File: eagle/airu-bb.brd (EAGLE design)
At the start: 86.4 x 54.6 mm, 34 parts, among them IC1 DS1307, U1 BMP180, U2 DHT22, U3 GPS, X2 53261-08, Y1 32.768kHz

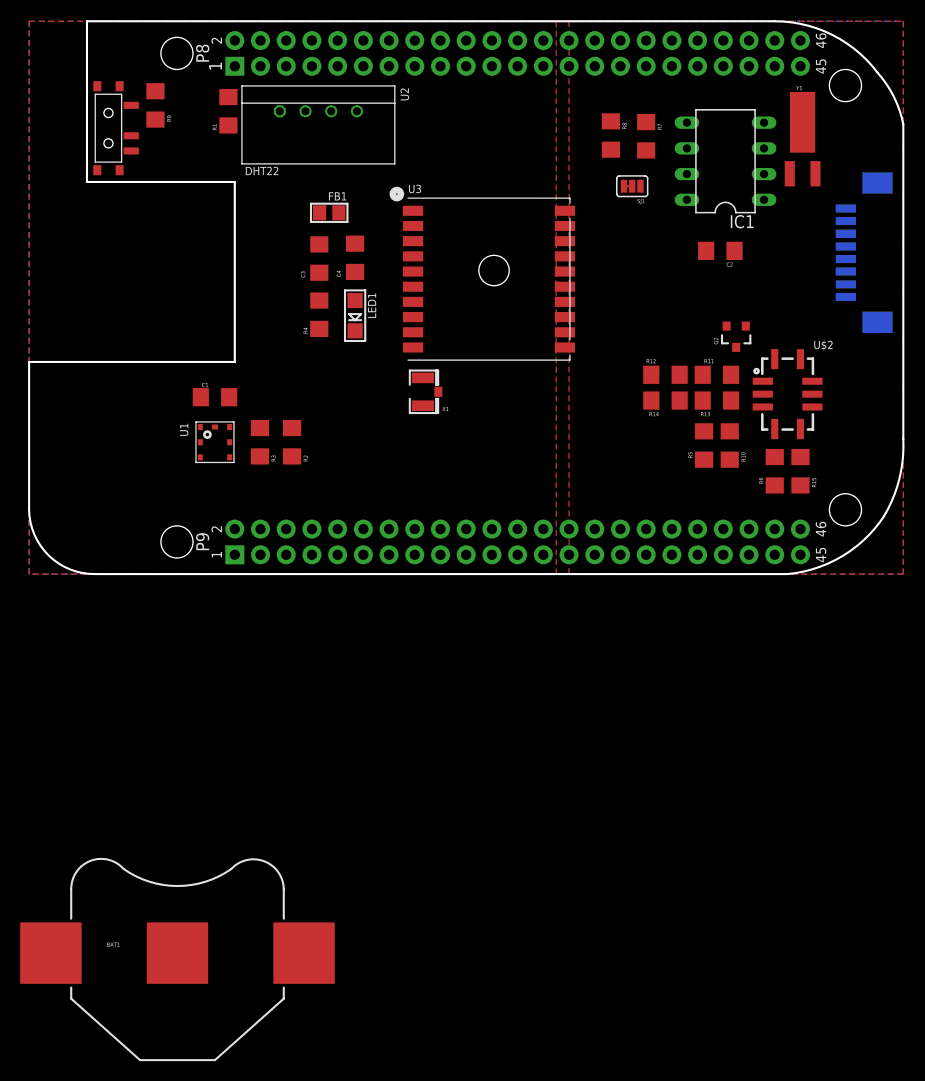
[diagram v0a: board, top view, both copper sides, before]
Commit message: Added modifications for AirU V2.0
This commit includes all modifications needed for AirU V2.0. This includes:

* Schematic additions integrating a mode button and real-time clock
* Board layout revisions to integrate the added components
* Changes to the BOM to reflect the new design

I also reorganized the repository structure.
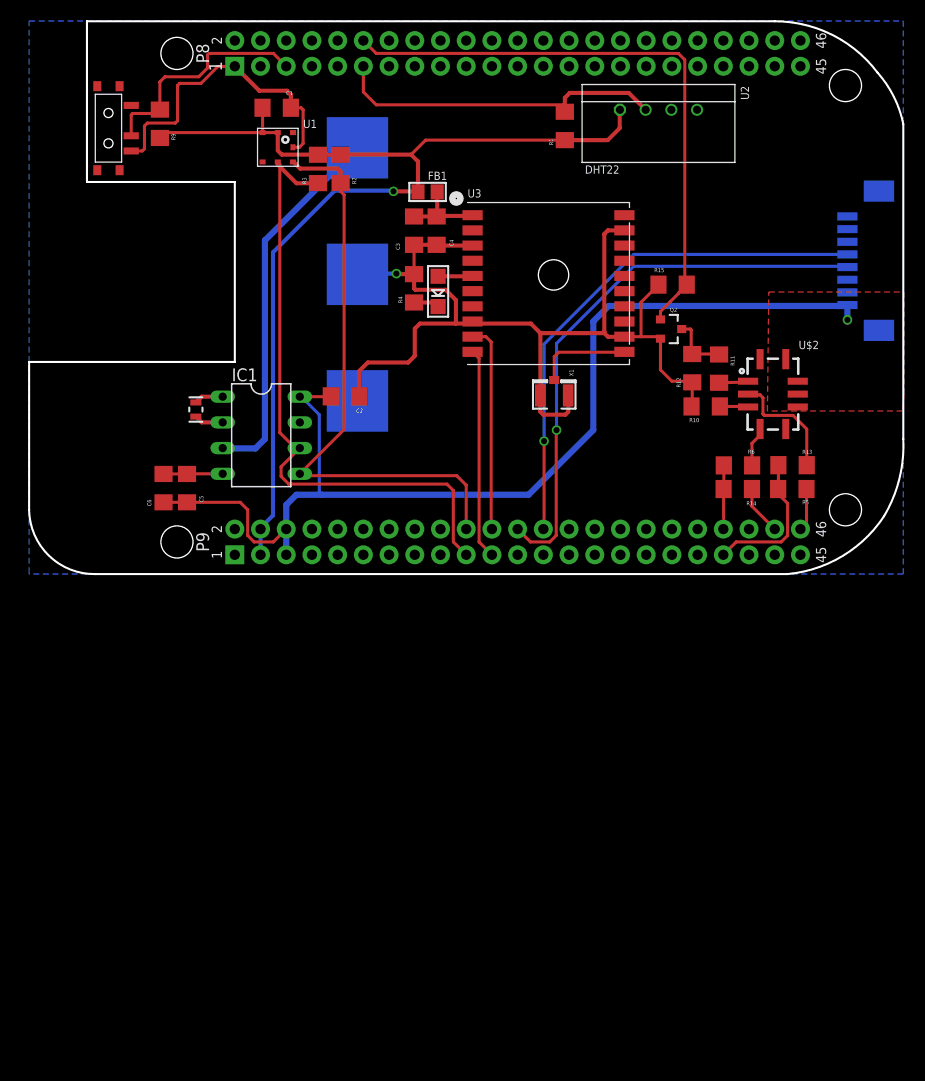
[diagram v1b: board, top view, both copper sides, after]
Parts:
- removed R7, R8: 10k, SparkFun-Passives:1206
- removed SJ1: JUMPER-PAD-3-2OF3_NC_BY_TRACE_SMALL, SparkFun-Passives:PAD-JUMPER-3-2OF3_NC_BY_TRACE_YES_SILK_FULL_BOX
- removed Y1: 32.768kHz, SparkFun-FreqCtrl:CRYSTAL-32KHZ-SMD
- added C5: 10uF, SparkFun-Passives:1206
- added C6: 0.1uF, SparkFun-Passives:1206
- added Y2: 32.768kHz, Lowduino:2-SMD
- moved BAT1 69.4 mm to (32.4, 29.6), flipped to the bottom, turned to 270 degrees
- moved IC1 53.3 mm to (22.9, 13.7), turned to 270 degrees
- moved C2 39.8 mm to (31.2, 17.6)
- moved U2 33.6 mm to (62.2, 45.9)
- moved R1 33.3 mm to (52.9, 44.3)
- moved U1 29.8 mm to (24.6, 42.2), turned to 0 degrees
- moved C1 29.2 mm to (24.5, 46.1)
- moved R3 27.6 mm to (28.5, 40.0)
- moved R2 27.4 mm to (30.8, 40.0)
- moved R15 22.3 mm to (63.6, 28.6), turned to 0 degrees
- moved X1 13.0 mm to (51.9, 17.6), turned to 90 degrees
- moved R14 11.3 mm to (70.0, 8.40), turned to 180 degrees
- moved FB1 9.94 mm to (39.4, 37.8), turned to 180 degrees
- moved R13 9.83 mm to (75.4, 10.8)
- moved C3 9.76 mm to (38.0, 33.9)
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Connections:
- removed net N$13: R7.2, SJ1.1
- removed net N$15: R8.2, SJ1.3
- net 5V: now also C5.2, C6.2; no longer SJ1.2
- net GND: now also C5.1, C6.1
- net N$12: now also Y2.1; no longer Y1.X2
- net N$14: now also Y2.2; no longer Y1.X1
- net SCL: no longer R8.1
- net SDA: no longer R7.1
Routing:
- net GND: track 0.00 -> 144.5 mm, vias 0 -> 1
- net 5V: track 0.00 -> 106.0 mm, vias 0 -> 1
- net 3.3V: track 0.00 -> 104.2 mm, vias 0 -> 1
- net SCL: track 0.00 -> 62.5 mm
- net PREHEAT_NOX: track 0.00 -> 59.3 mm
- net SDA: track 0.00 -> 58.2 mm
- net PM_RXD: track 0.00 -> 55.5 mm, vias 0 -> 1
- net PM_TXD: track 0.00 -> 51.9 mm, vias 0 -> 1
- net N$11: track 0.00 -> 37.1 mm
- net DHT_DATA: track 0.00 -> 33.3 mm
- net OP_MODE: track 0.00 -> 22.8 mm
- net GPS_RX: track 0.00 -> 20.8 mm
- net GPS_TX: track 0.00 -> 20.6 mm
- net VOX: track 0.00 -> 14.5 mm
- net N$6: track 0.00 -> 11.7 mm
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- removed copper zone on layer 1, net 3.3V
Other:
- board text added: "Lab/Field"
